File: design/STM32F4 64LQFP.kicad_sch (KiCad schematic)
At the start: 15 parts, among them P2 SWD, U1 STM32F40X_LQFP64, X2 8MHz 10ppm

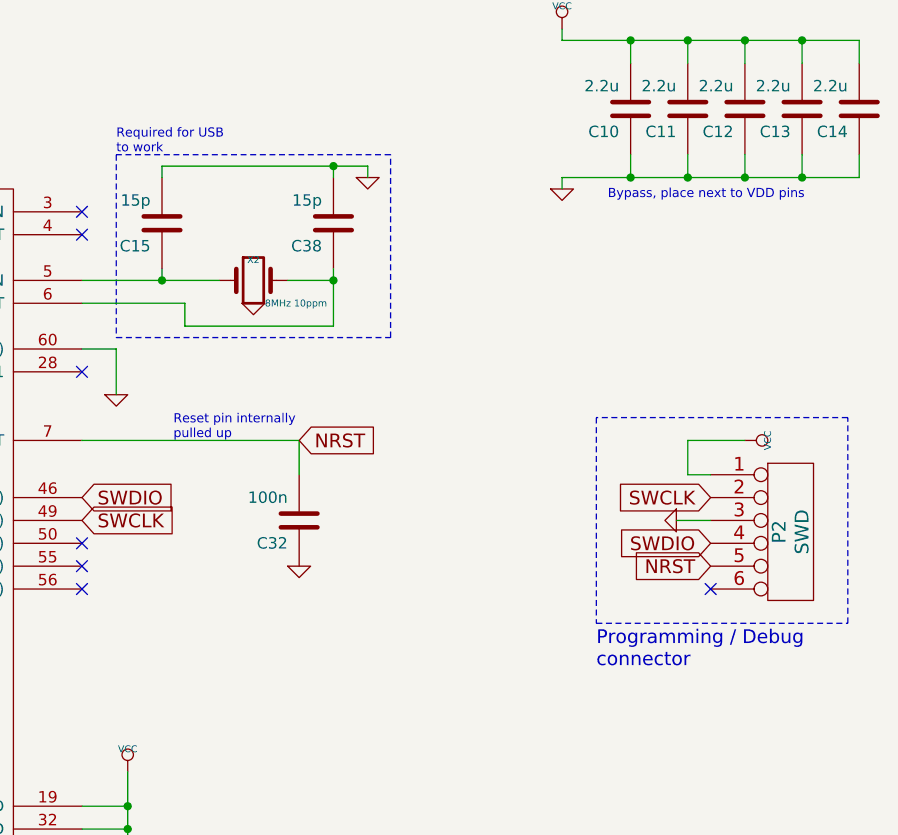
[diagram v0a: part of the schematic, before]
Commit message: v 4.13 produced by jlcpcb
Some serious issues with usb connectors facing the caps. Working fine
otherwise
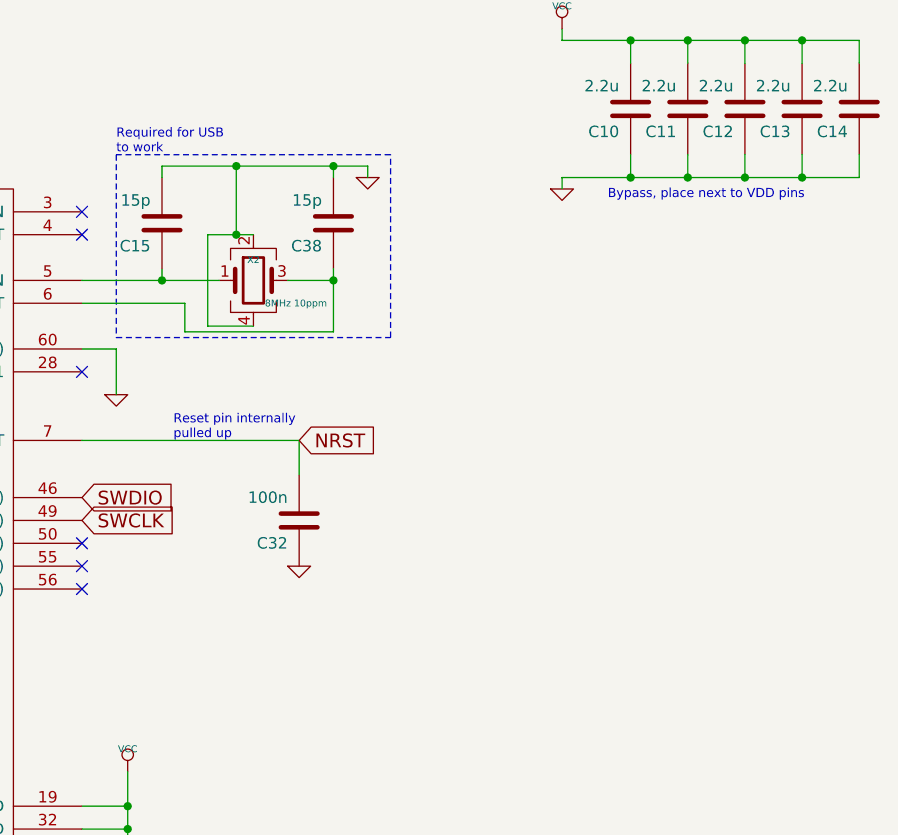
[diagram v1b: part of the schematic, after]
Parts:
- removed P2: SWD, CRF1:MICRO_JST_6, symbol BLDC_4-rescue:CONN_6
- C10, C11, C12, C13, C14, C16, C17, C31, C35: JLCPCB (none) -> C23630
- U1: JLCPCB (none) -> C15742
- X2: symbol Device:Crystal -> Device:Crystal_GND24; JLCPCB (none) -> C5308002
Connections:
- net GND: now also X2.2, X2.4
- net at C38.1, U1.6 (PH1-OSC_OUT): now also X2.3; no longer X2.2
- no-connect marks 13 -> 12
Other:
- note removed: "Programming / Debug connector"
